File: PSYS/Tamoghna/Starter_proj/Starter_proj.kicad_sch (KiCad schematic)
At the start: 13 parts, among them U1 STM32WB55CEUx

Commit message: without history test
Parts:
- added Y1: 32Mhz, symbol Device:Crystal
- added Y2: 32kHz768, symbol Device:Crystal
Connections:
- net smpsfb: now reaches C10.1, L2.2, U1.31 (VFBSMPS)
- net smplx: now reaches L1.1, U1.33 (VLXSMPS)
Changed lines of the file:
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@@
+		)
+	)
+	(label "smplx"
+		(at 167.64 55.88 0)
+		(effects
+			(font
+				(size 1.27 1.27)
+			)
+			(justify left bottom)
+		)
+	)
+	(label "smpsfb"
+		(at 167.64 68.58 0)
+		(effects
+			(font
+				(size 1.27 1.27)
+			)
+			(justify left bottom)
 		)
 	)
@@
 	)
 	(symbol
+		(lib_id "Device:Crystal")
+		(at 177.8 87.63 0)
+		(unit 1)
+		(body_style 1)
+		(exclude_from_sim no)
+		(in_bom yes)
+		(on_board yes)
+		(in_pos_files yes)
+		(dnp no)
+		(fields_autoplaced yes)
+		(property "Reference" "Y1"
+			(at 177.8 80.01 0)
+			(show_name no)
+			(do_not_autoplace no)
+			(effects
+				(font
+					(size 1.27 1.27)
+				)
+			)
+		)
+		(property "Value" "32Mhz"
+			(at 177.8 82.55 0)
+			(show_name no)
+			(do_not_autoplace no)
+			(effects
+				(font
+					(size 1.27 1.27)
+				)
+			)
+		)
+		(property "Footprint" ""
+			(at 177.8 87.63 0)
+			(hide yes)
+			(show_name no)
+			(do_not_autoplace no)
+			(effects
+				(font
+					(size 1.27 1.27)
+				)
+			)
+		)
+		(property "Datasheet" ""
+			(at 177.8 87.63 0)
+			(hide yes)
+			(show_name no)
+			(do_not_autoplace no)
+			(effects
+				(font
+					(size 1.27 1.27)
+				)
+			)
+		)
+		(property "Description" "Two pin crystal"
+			(at 177.8 87.63 0)
+			(hide yes)
+			(show_name no)
+			(do_not_autoplace no)
+			(effects
+				(font
+					(size 1.27 1.27)
+				)
+			)
+		)
+		(pin "1"
+		)
+		(pin "2"
+		)
+		(instances
+			(project "Starter_proj"
+				(path "/aec4b483-69a6-4875-8257-bb74b432c214"
+					(reference "Y1")
+					(unit 1)
+				)
+			)
+		)
+	)
+	(symbol
 		(lib_id "Device:C")
 		(at 69.85 44.45 0)
@@
 					(unit 1)
 				)
+			)
+		)
+	)
+	(symbol
+		(lib_id "Device:Crystal")
+		(at 189.23 87.63 0)
+		(unit 1)
+		(body_style 1)
+		(exclude_from_sim no)
+		(in_bom yes)
+		(on_board yes)
+		(in_pos_files yes)
+		(dnp no)
+		(fields_autoplaced yes)
+		(property "Reference" "Y2"
+			(at 189.23 80.01 0)
+			(show_name no)
+			(do_not_autoplace no)
+			(effects
+				(font
+					(size 1.27 1.27)
+				)
+			)
+		)
+		(property "Value" "32kHz768"
+			(at 189.23 82.55 0)
+			(show_name no)
+			(do_not_autoplace no)
+			(effects
+				(font
+					(size 1.27 1.27)
+				)
+			)
+		)
+		(property "Footprint" ""
+			(at 189.23 87.63 0)
+			(hide yes)
+			(show_name no)
+			(do_not_autoplace no)
+			(effects
+				(font
+					(size 1.27 1.27)
+				)
+			)
+		)
+		(property "Datasheet" ""
+			(at 189.23 87.63 0)
+			(hide yes)
+			(show_name no)
+			(do_not_autoplace no)
+			(effects
+				(font
+					(size 1.27 1.27)
+				)
+			)
+		)
+		(property "Description" "Two pin crystal"
+			(at 189.23 87.63 0)
+			(hide yes)
+			(show_name no)
+			(do_not_autoplace no)
+			(effects
+				(font
+					(size 1.27 1.27)
+				)
+			)
+		)
+		(pin "1"
+		)
+		(pin "2"
+		)
+		(instances
+			(project "Starter_proj"
+				(path "/aec4b483-69a6-4875-8257-bb74b432c214"
+					(reference "Y2")
+					(unit 1)
+				)

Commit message: clock done
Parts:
- added C11, C12: 10p, symbol Device:C
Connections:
- net GND: now also C11.2, C12.2
- net at Y1.1: now also U1.24 (OSC_OUT)
- net at Y1.2: now also U1.25 (OSC_IN)
- net at Y2.1: now also U1.3 (PC15), C12.1
- net at Y2.2: now also U1.2 (PC14), C11.1
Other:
- moved on the sheet: Y1, Y2

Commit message: RF done
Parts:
- added C13: 0p8, symbol Device:C
- added C14: 0p3, symbol Device:C
- added FLT1: DLF162500LT-5028A1, footprintlib:Untitled, symbol New_Library:DLF162500LT-5028A1
- added J1: Conn_Coaxial, symbol Connector:Conn_Coaxial
- added L3: L, Package_SO:SOIC-16_3.9x9.9mm_P1.27mm, symbol Device:L
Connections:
- net GND: now also C10.2, C13.2, C14.2, FLT1.2 (GND), FLT1.4 (GND), J1.2 (Ext)
- net smpsfb: now also U1.24 (OSC_OUT), Y1.1
- net at U1.21 (RF1): now also C13.1, L3.1
- new net: C14.1, FLT1.1 (IN), L3.2
- new net: FLT1.3 (OUT), J1.1 (In)
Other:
- moved on the sheet: Y1

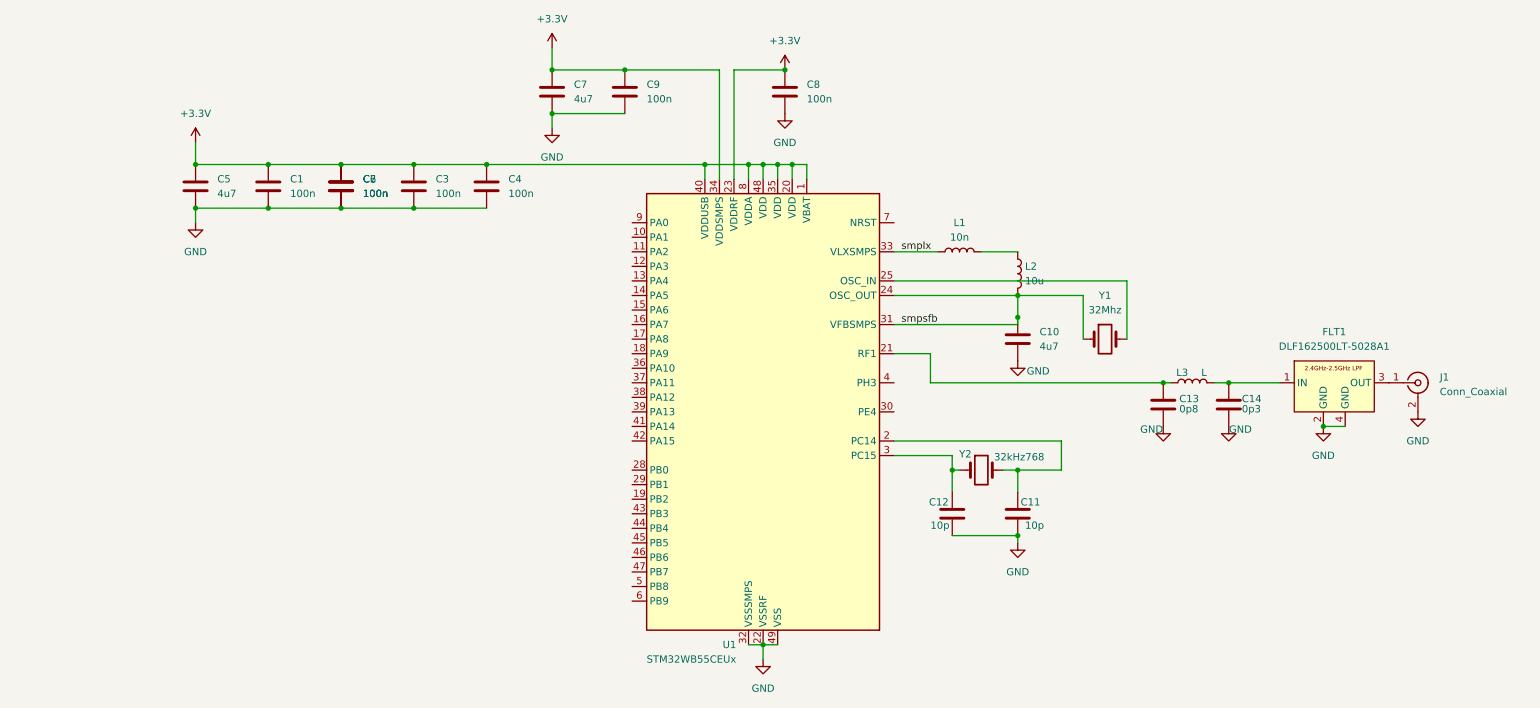
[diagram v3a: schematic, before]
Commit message: programInterface done
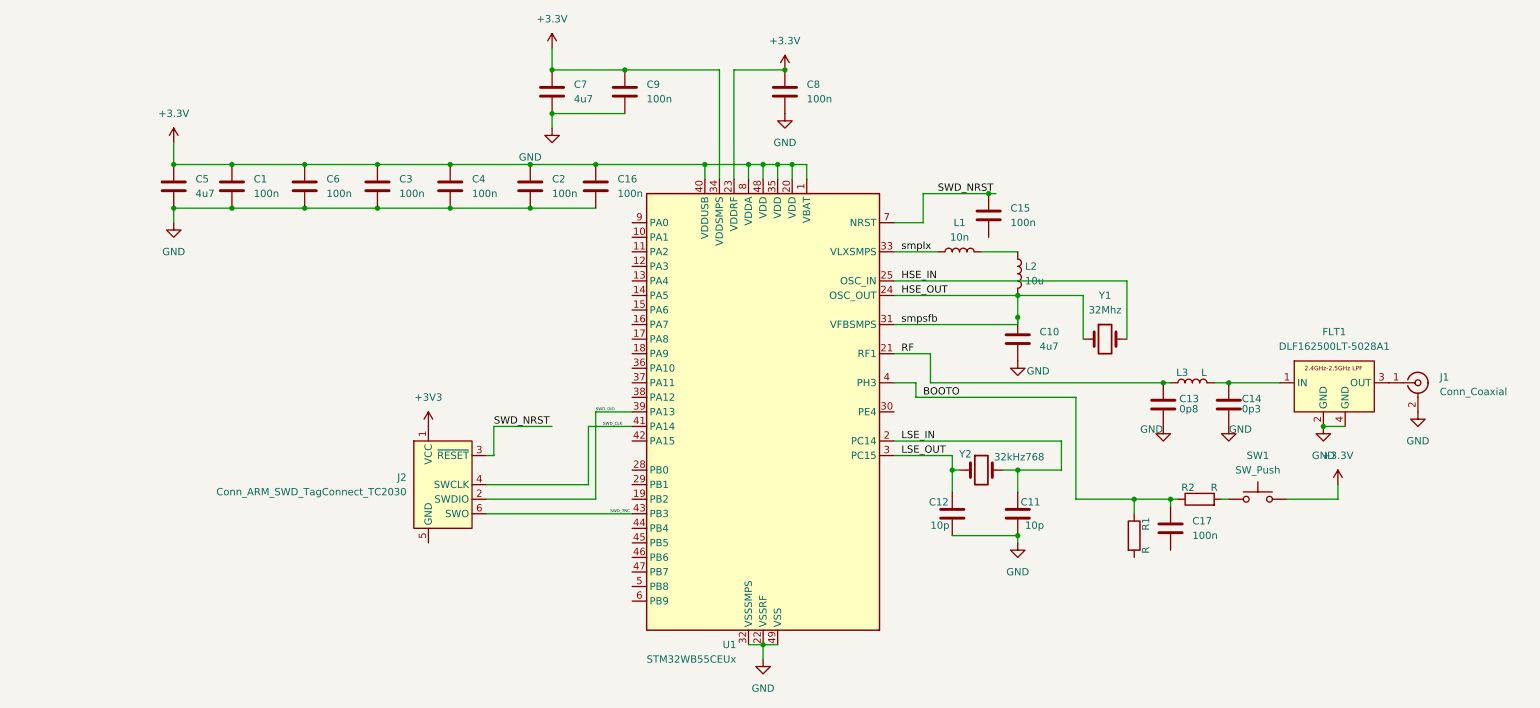
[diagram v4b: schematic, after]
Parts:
- added C15, C16, C17: 100n, symbol Device:C
- added J2: Conn_ARM_SWD_TagConnect_TC2030, Connector:Tag-Connect_TC2030-IDC-FP_2x03_P1.27mm_Vertical, symbol Connector:Conn_ARM_SWD_TagConnect_TC2030
- added R1, R2: R, symbol Device:R
- added SW1: SW_Push, Button_Switch_THT:SW_NKK_GW12LJP, symbol Switch:SW_Push
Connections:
- net +3.3V: now also C16.1, SW1.2
- net GND: now also C16.2
- net HSE_IN: now reaches U1.25 (OSC_IN), Y1.2
- net RF: now reaches C13.1, L3.1, U1.21 (RF1)
- net LSE_IN: now reaches C11.1, U1.2 (PC14), Y2.2
- net LSE_OUT: now reaches C12.1, U1.3 (PC15), Y2.1
- net SWD_DIO: now reaches U1.39 (PA13)
- net SWD_DIO: now also J2.2 (SWDIO)
- net BOOTO: now reaches U1.4 (PH3)
- net BOOTO: now also C17.1, R1.1, R2.1
- net SWD_CLK: now reaches U1.41 (PA14)
- net SWD_CLK: now also J2.4 (SWCLK)
- net SWD_TRC: now reaches U1.43 (PB3)
- net SWD_TRC: now also J2.6 (SWO)
- net SWD_NRST: now reaches U1.7 (NRST)
- net SWD_NRST: now also C15.1, J2.3 (~{RESET})
- net smpsfb renamed HSE_OUT
- new net: R2.2, SW1.1
- new net +3V3: J2.1 (VCC)
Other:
- moved on the sheet: C1, C2, C3, C4, C5, C6

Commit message: USB done
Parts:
- added J3: USB_C_Receptacle_USB2.0_16P, symbol Connector:USB_C_Receptacle_USB2.0_16P
- added R3, R4: 5K1, symbol Device:R
- added U2: USBLC6-2SC6, Package_TO_SOT_SMD:SOT-23-6, symbol Power_Protection:USBLC6-2SC6
- R1: value R -> 5k1
- R2: value R -> 100R
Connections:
- net GND: now also C15.2, C17.2, J2.5 (GND), R1.2, J3.A1 (GND), J3.A12 (GND), J3.B1 (GND), J3.B12 (GND), J3.SH (SHIELD), R3.2, R4.2, U2.2 (GND)
- net USB_D-: now reaches U1.37 (PA11)
- net USB_D-: now also U2.6 (I/O1)
- net USB_D+: now reaches U1.38 (PA12)
- net USB_D+: now also U2.4 (I/O2)
- new net: J3.B5 (CC2), R3.1
- new net: J3.A5 (CC1), R4.1
- new net: J3.A4 (VBUS), J3.A9 (VBUS), J3.B4 (VBUS), J3.B9 (VBUS), U2.5 (VBUS)
- new net: J3.A6 (D+), J3.B6 (D+), U2.3 (I/O2)
- new net: J3.A7 (D-), J3.B7 (D-), U2.1 (I/O1)
- no-connect marks 0 -> 3
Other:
- moved on the sheet: C15

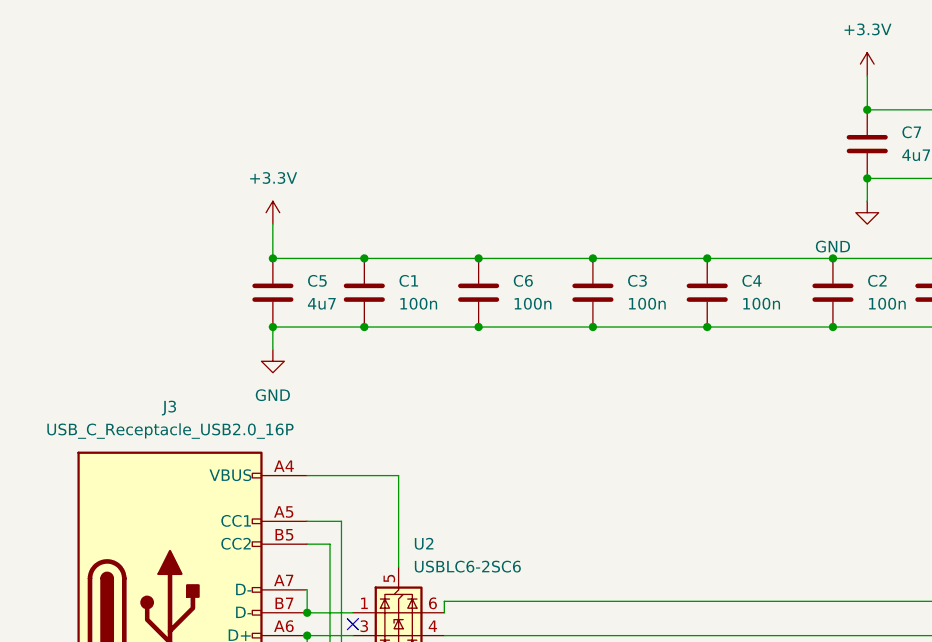
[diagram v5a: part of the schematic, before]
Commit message: LDO regulator
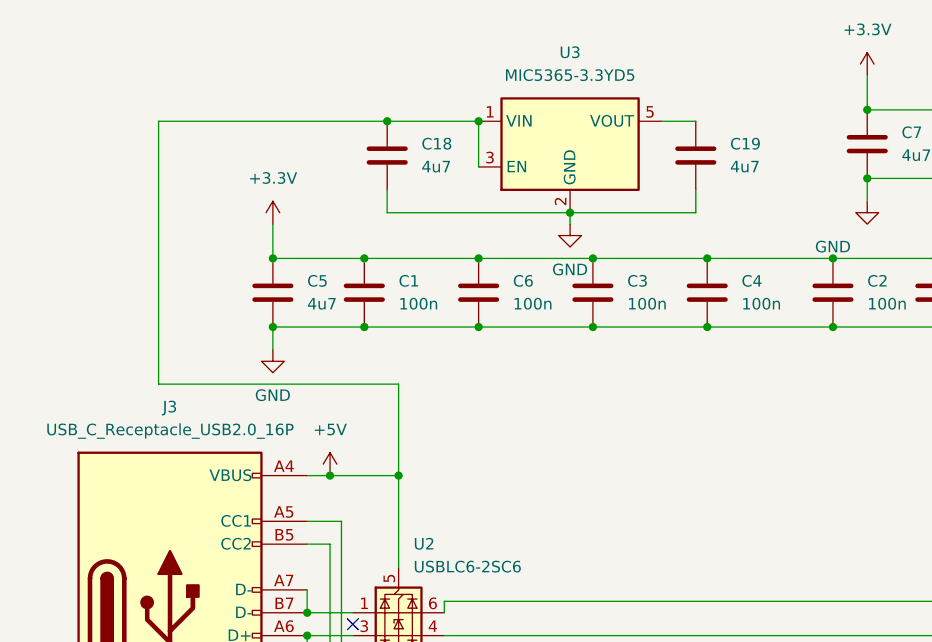
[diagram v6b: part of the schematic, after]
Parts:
- added C18, C19: 4u7, Package_TO_SOT_SMD:TSOT-23-5, symbol Device:C
- added U3: MIC5365-3.3YD5, Package_TO_SOT_SMD:TSOT-23-5, symbol Regulator_Linear:MIC5365-3.3YD5
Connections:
- net GND: now also C18.2, C19.2, U3.2 (GND)
- net +5V: now reaches J3.A4 (VBUS), J3.A9 (VBUS), J3.B4 (VBUS), J3.B9 (VBUS), U2.5 (VBUS)
- net +5V: now also C18.1, U3.1 (VIN), U3.3 (EN)
- new net: C19.1, U3.5 (VOUT)

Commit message: middle stuff
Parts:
- added J4: Conn_01x04, symbol Connector_Generic:Conn_01x04
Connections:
- net UART_TX: now reaches U1.11 (PA2)
- net UART_RX: now reaches U1.12 (PA3)
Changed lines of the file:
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@@
 	(wire
 		(pts
+			(xy 111.76 58.42) (xy 120.65 58.42)
+		)
+		(stroke
+			(width 0)
+			(type default)
+		)
+	)
+	(wire
+		(pts
 			(xy 171.45 40.64) (xy 184.15 40.64)
 		)
@@
 	(wire
 		(pts
+			(xy 111.76 55.88) (xy 120.65 55.88)
+		)
+		(stroke
+			(width 0)
+			(type default)
+		)
+	)
+	(wire
+		(pts
 			(xy 133.35 40.64) (xy 140.97 40.64)
 		)
@@
 		)
 	)
+	(label "UART_TX"
+		(at 111.76 55.88 0)
+		(effects
+			(font
+				(size 1.27 1.27)
+			)
+			(justify left bottom)
+		)
+	)
+	(label "UART_RX"
+		(at 111.76 58.42 0)
+		(effects
+			(font
+				(size 1.27 1.27)
+			)
+			(justify left bottom)
+		)
+	)
 	(label "SWD_TRC"
 		(at 116.84 101.6 0)
@@
 					(unit 1)
 				)
+			)
+		)
+	)
+	(symbol
+		(lib_id "Connector_Generic:Conn_01x04")
+		(at 82.55 58.42 0)
+		(unit 1)
+		(body_style 1)
+		(exclude_from_sim no)
+		(in_bom yes)
+		(on_board yes)
+		(in_pos_files yes)
+		(dnp no)
+		(property "Reference" "J4"
+			(at 82.042 53.34 0)
+			(show_name no)
+			(do_not_autoplace no)
+			(effects
+				(font
+					(size 1.27 1.27)
+				)
+				(justify left)
+			)
+		)
+		(property "Value" "Conn_01x04"
+			(at 77.216 65.786 0)
+			(show_name no)
+			(do_not_autoplace no)
+			(effects
+				(font
+					(size 1.27 1.27)
+				)
+				(justify left)
+			)
+		)
+		(property "Footprint" ""
+			(at 82.55 58.42 0)
+			(hide yes)
+			(show_name no)
+			(do_not_autoplace no)
+			(effects
+				(font
+					(size 1.27 1.27)
+				)
+			)
+		)
+		(property "Datasheet" ""
+			(at 82.55 58.42 0)
+			(hide yes)
+			(show_name no)
+			(do_not_autoplace no)
+			(effects
+				(font
+					(size 1.27 1.27)
+				)
+			)
+		)
+		(property "Description" "Generic connector, single row, 01x04, script generated (kicad-library-utils/schlib/autogen/connector/)"
+			(at 82.55 58.42 0)
+			(hide yes)
+			(show_name no)
+			(do_not_autoplace no)
+			(effects
+				(font
+					(size 1.27 1.27)
+				)
+			)
+		)
+		(pin "3"
+		)
+		(pin "4"
+		)
+		(pin "1"
+		)
+		(pin "2"
+		)
+		(instances
+			(project "Starter_proj"
+				(path "/aec4b483-69a6-4875-8257-bb74b432c214"
+					(reference "J4")
+					(unit 1)
+				)

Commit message: i dont wanna redo annotation i will do it later AHHHHHHHHHHHHHH
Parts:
- added D1: LED, symbol Device:LED
- added R5, R6, R7: 220R, symbol Device:R
- R2: value 100R -> 220R
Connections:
- net +3V3: now also J4.1 (Pin_1)
- net GND: now also J4.4 (Pin_4), R7.1
- net UART_RX: now also R6.2
- net UART_TX: now also R5.2
- net LED_A: now reaches U1.16 (PA7)
- net LED_A: now also D1.2 (A)
- net UART_TXC: now reaches J4.2 (Pin_2)
- net UART_TXC: now also R5.1
- net UART_RXC: now reaches J4.3 (Pin_3)
- net UART_RXC: now also R6.1
- new net LED_K: D1.1 (K), R7.2
- no-connect marks 3 -> 22
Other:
- note added: "+5v to +3v3 LDO Regulator"
- note added: "BOOTO Switch"
- note added: "HSE Crystal"
- note added: "LSE Crystal"
- note added: "RF & u.FL Connector"
- note added: "STM32WB55 MCU"
- note added: "SWD Header"
- note added: "UART Header"
- note added: "USB C connector"
- company: (none) -> LHR Solar
- title: (none) -> Starter Proj STM32 MCU board
- moved on the sheet: J4
